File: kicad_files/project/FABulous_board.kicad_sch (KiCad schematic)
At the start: 5 parts, among them P1 USB_C_Plug_USB2.0

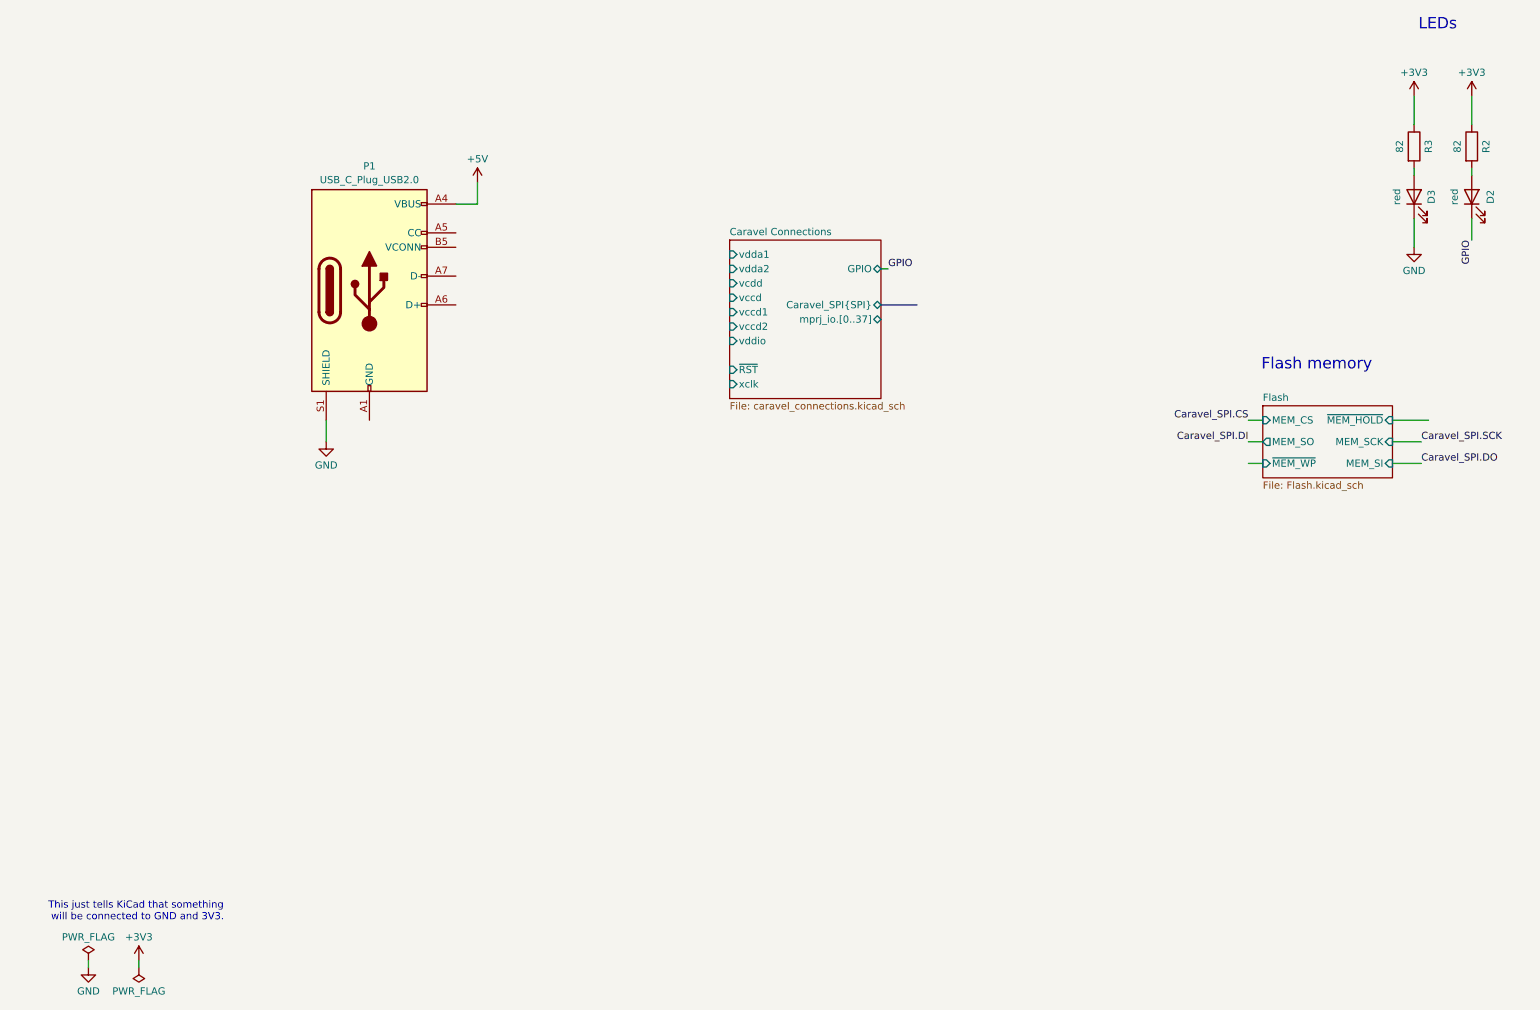
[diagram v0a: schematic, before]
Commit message: feat: schematic almost done, also add all footprints and symbol libraries except for external libraries
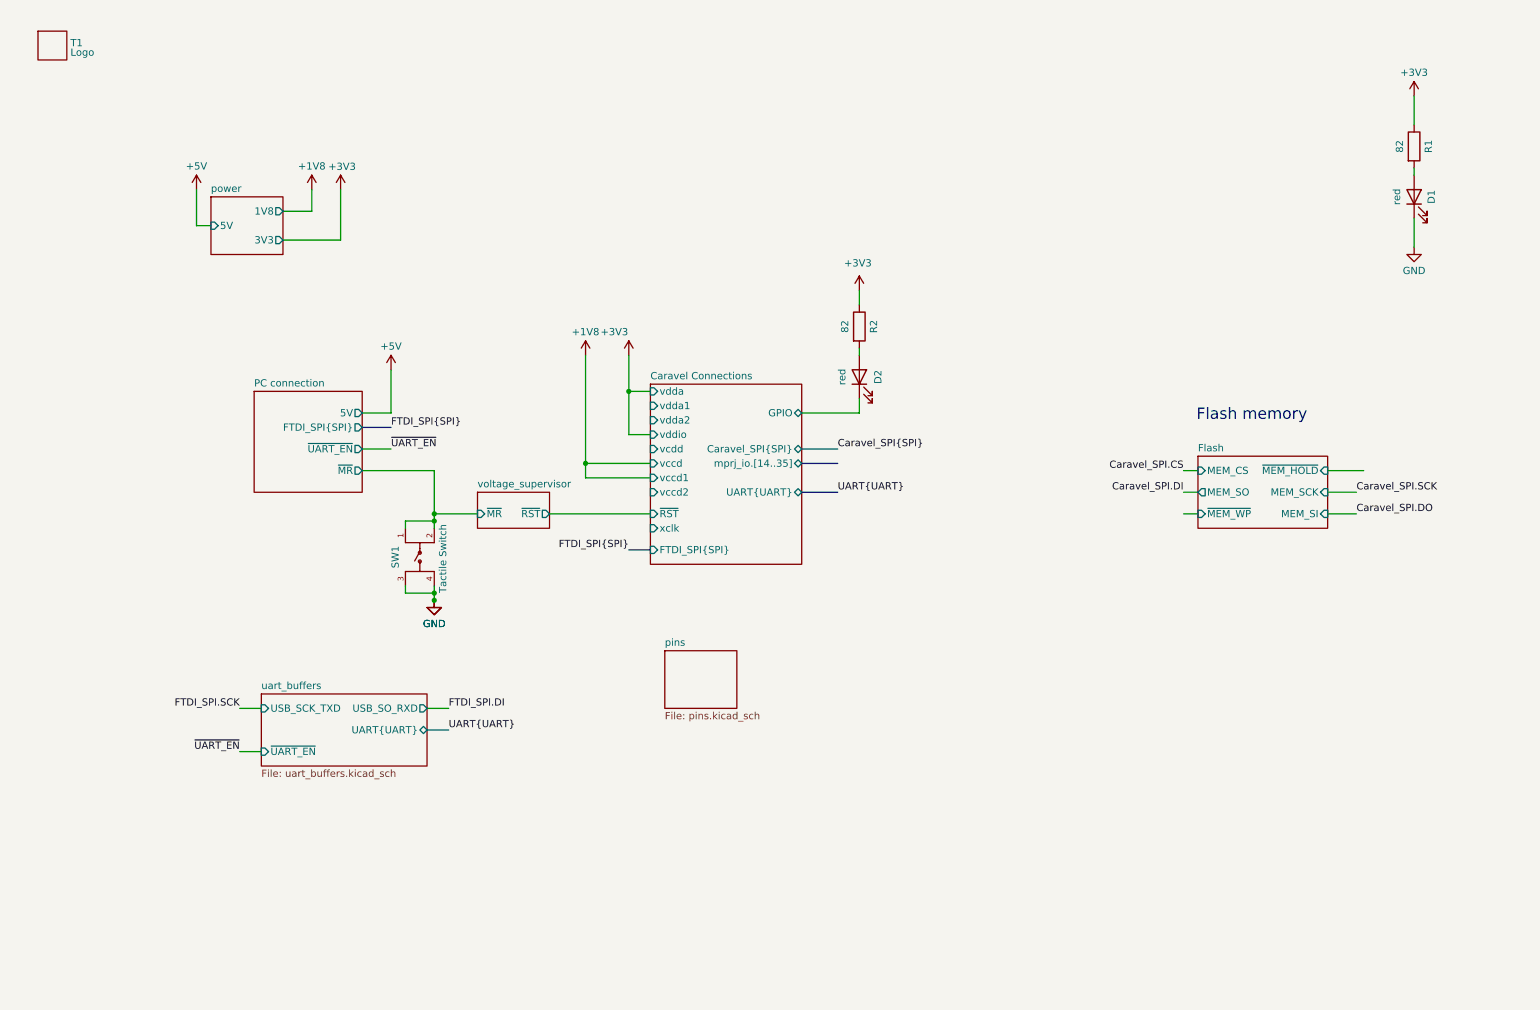
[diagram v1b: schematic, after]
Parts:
- removed P1: USB_C_Plug_USB2.0, symbol Connector:USB_C_Plug_USB2.0
- added SW1: Tactile Switch, easy_eda:SW_SMD_4P_L6.0_W6.0-P4.5-LS8.6, symbol easy_eda:Tactile Switch
- added T1: Logo, FABulous:logo, symbol FABulous:logo
- renumbered D3 to D1, R3 to R1
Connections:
- net GND: now also SW1.3, SW1.4
- net GPIO renamed Caravel Connections/GPIO
- new net PC connection/~{MR}: SW1.1, SW1.2
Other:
- added sheet PC connection (pc_connection.kicad_sch)
- added sheet pins (pins.kicad_sch)
- added sheet power (power.kicad_sch)
- added sheet uart_buffers (uart_buffers.kicad_sch)
- added sheet voltage_supervisor (voltage_supervisor.kicad_sch)
- sheet Caravel Connections ports: added FTDI_SPI{SPI}, UART{UART}, mprj_io.[14..35], vdda; removed mprj_io.[0..37]
- note removed: "LEDs"
- note removed: "This just tells KiCad that something will be connected to GND and 3V3."
- moved on the sheet: D2, R2

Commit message: started with board layout, also added more stuff on the schematic
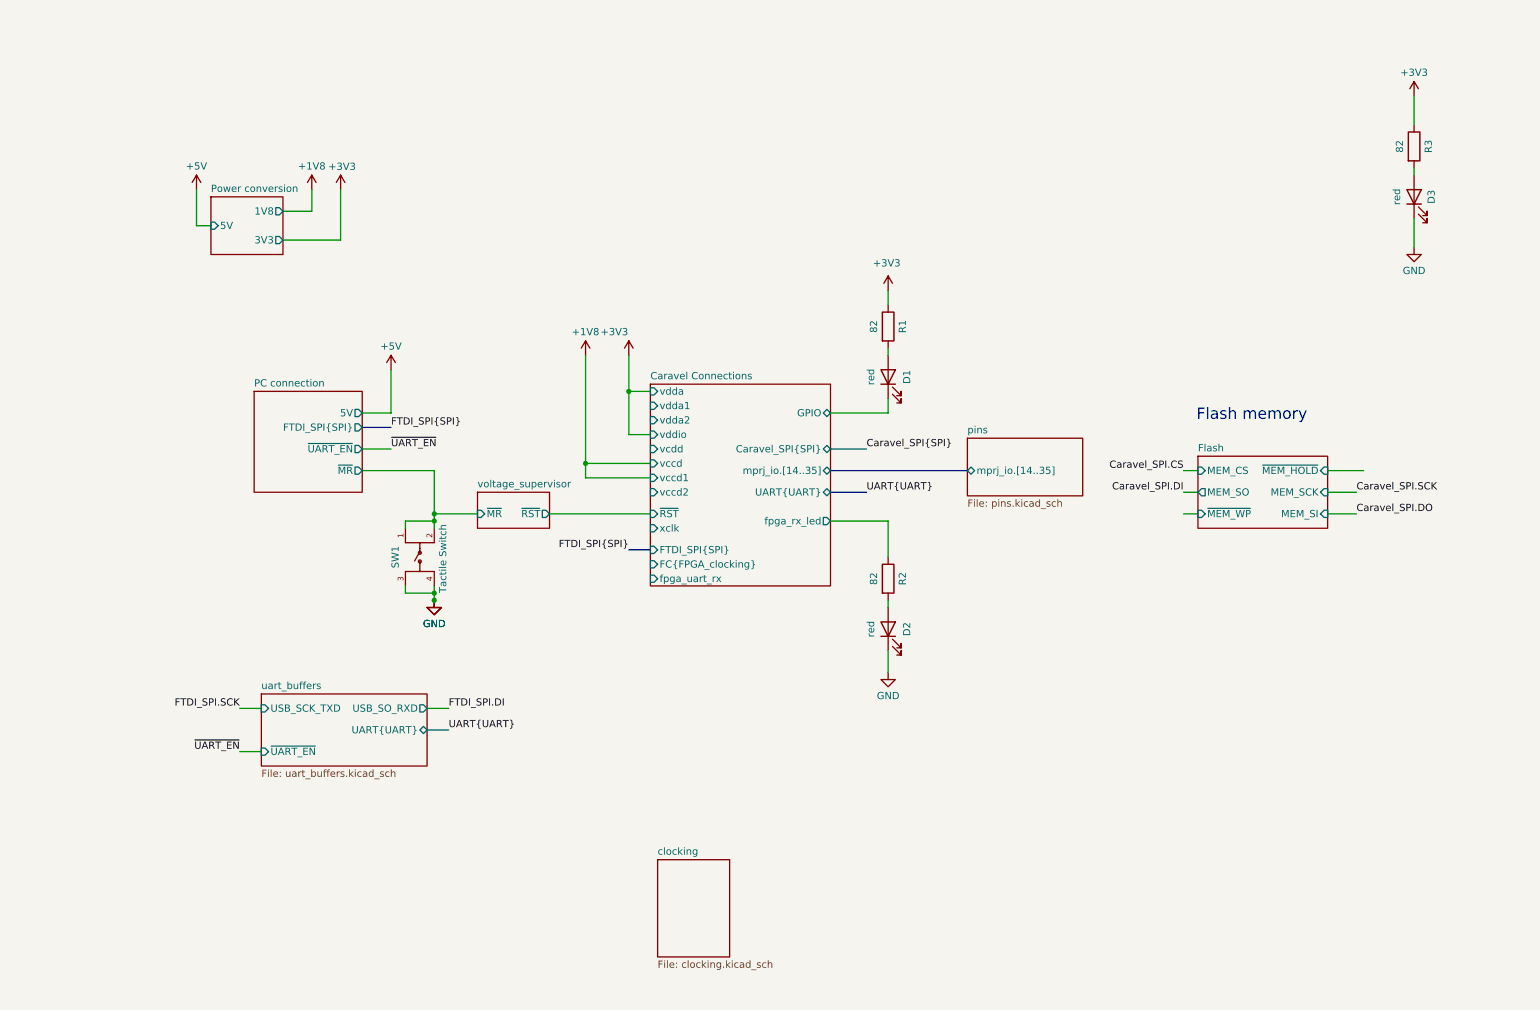
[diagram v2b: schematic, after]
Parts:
- removed T1: Logo, FABulous:logo, symbol FABulous:logo
- added D2: red, LED_SMD:LED_1206_3216Metric, symbol Device:LED
- added R2: 82, Resistor_SMD:R_0805_2012Metric, symbol Device:R
- renumbered D2 to D1, D1 to D3, R2 to R1, R1 to R3
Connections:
- net GND: now also D2.1 (K)
- new net: D2.2 (A), R2.2
- new net Caravel Connections/fpga_rx_led: R2.1
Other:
- sheet power renamed Power conversion
- added sheet clocking (clocking.kicad_sch)
- sheet Caravel Connections ports: added FC{FPGA_clocking}, fpga_rx_led, fpga_uart_rx; removed none
- sheet pins ports: added mprj_io.[14..35]; removed none
- moved on the sheet: D1, R1

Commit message: clocking IC to the schematic with all needed connections, clocks still have to be connected
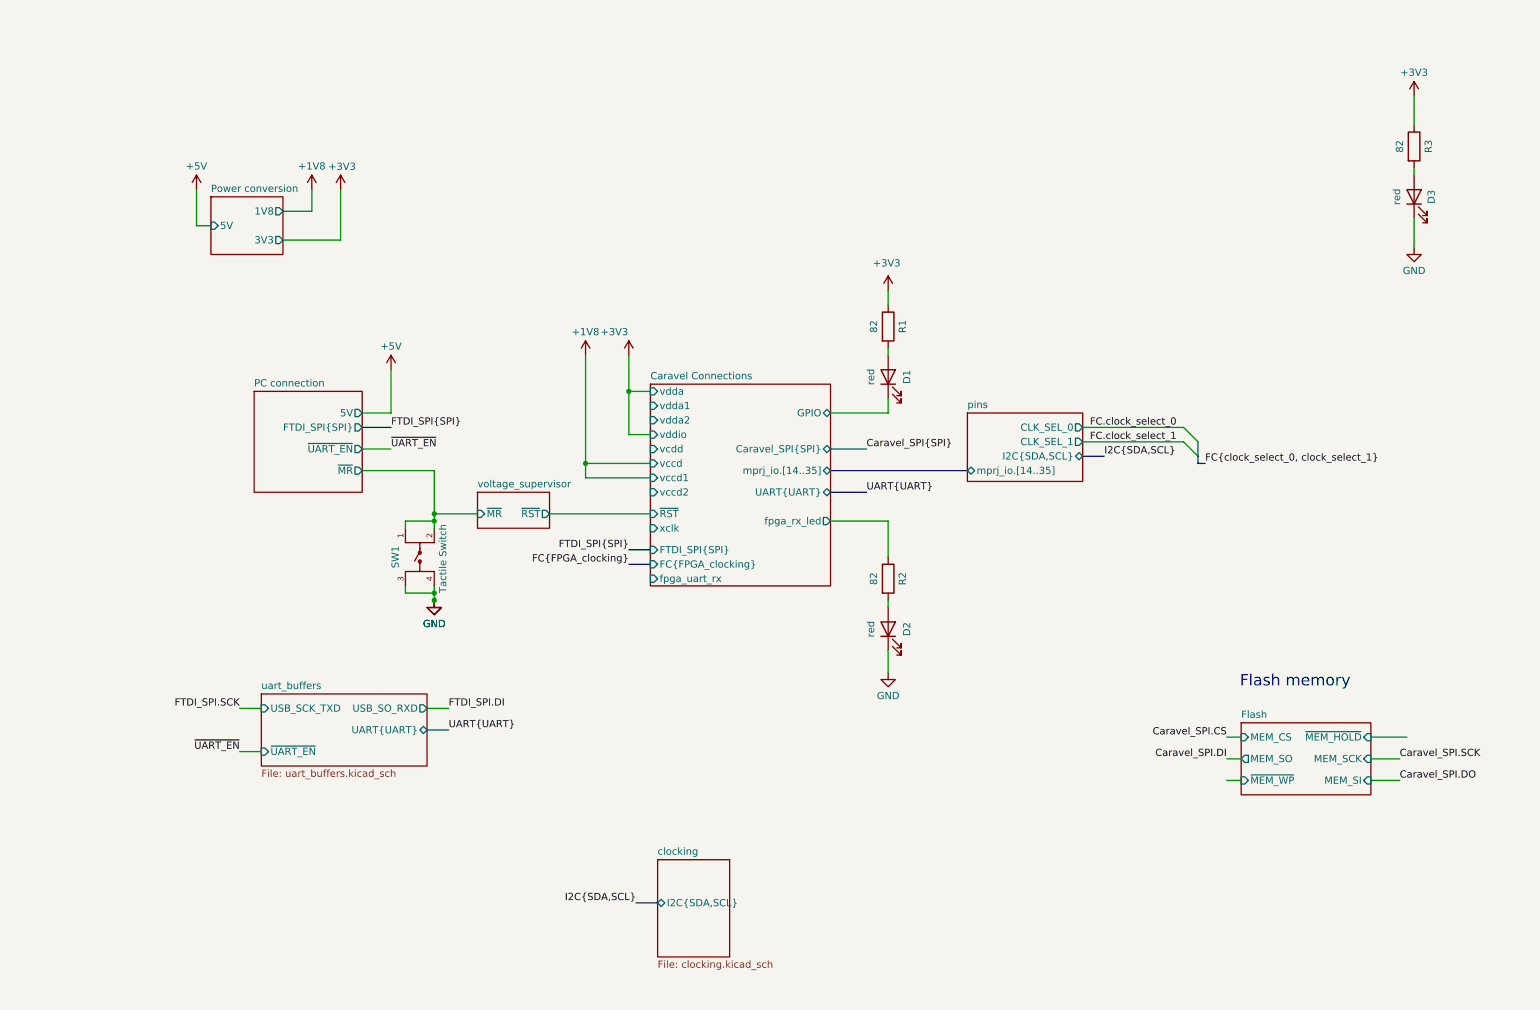
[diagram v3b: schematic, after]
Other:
- sheet clocking ports: added I2C{SDA,SCL}; removed none
- sheet pins ports: added CLK_SEL_0, CLK_SEL_1, I2C{SDA,SCL}; removed none

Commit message: new layout, add more pin header, change the caravel power pin supply
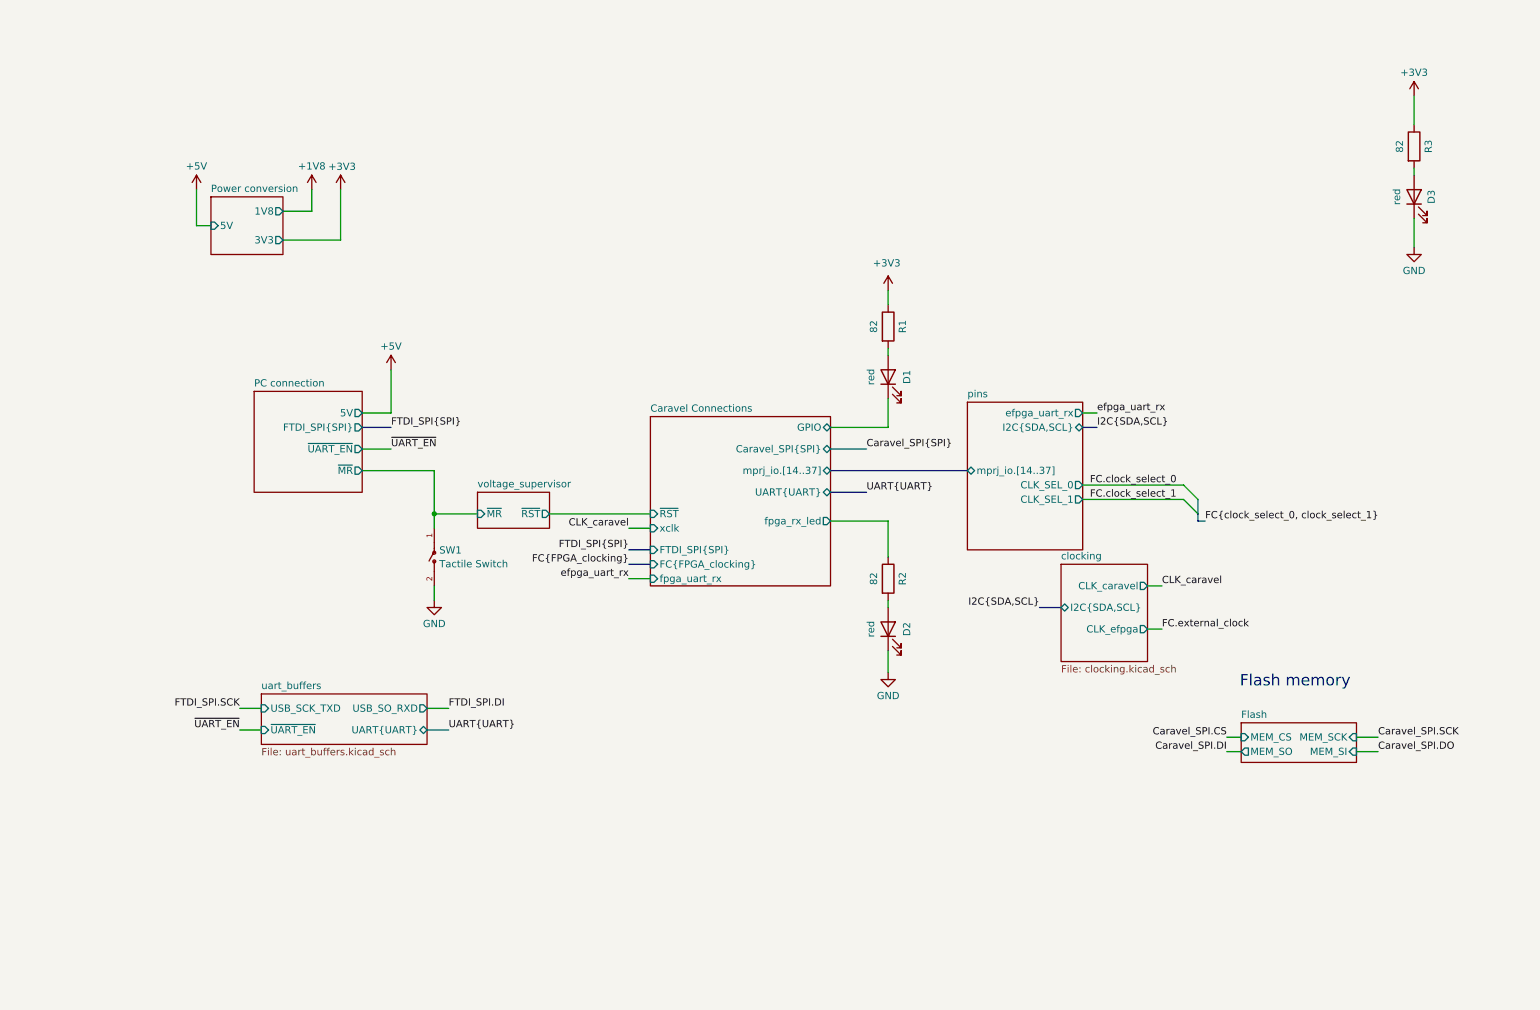
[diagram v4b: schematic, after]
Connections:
- net GND: now also SW1.2; no longer SW1.3
- net PC connection/~{MR}: now also SW1.3; no longer SW1.2
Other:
- sheet Caravel Connections ports: added mprj_io.[14..37]; removed mprj_io.[14..35], vccd, vccd1, vccd2, vcdd, vdda, vdda1, vdda2, vddio
- sheet Flash ports: added none; removed ~{MEM_HOLD}, ~{MEM_WP}
- sheet clocking ports: added CLK_caravel, CLK_efpga; removed none
- sheet pins ports: added efpga_uart_rx, mprj_io.[14..37]; removed mprj_io.[14..35]

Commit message: misc: simplifiy power pins and other components, add test pins
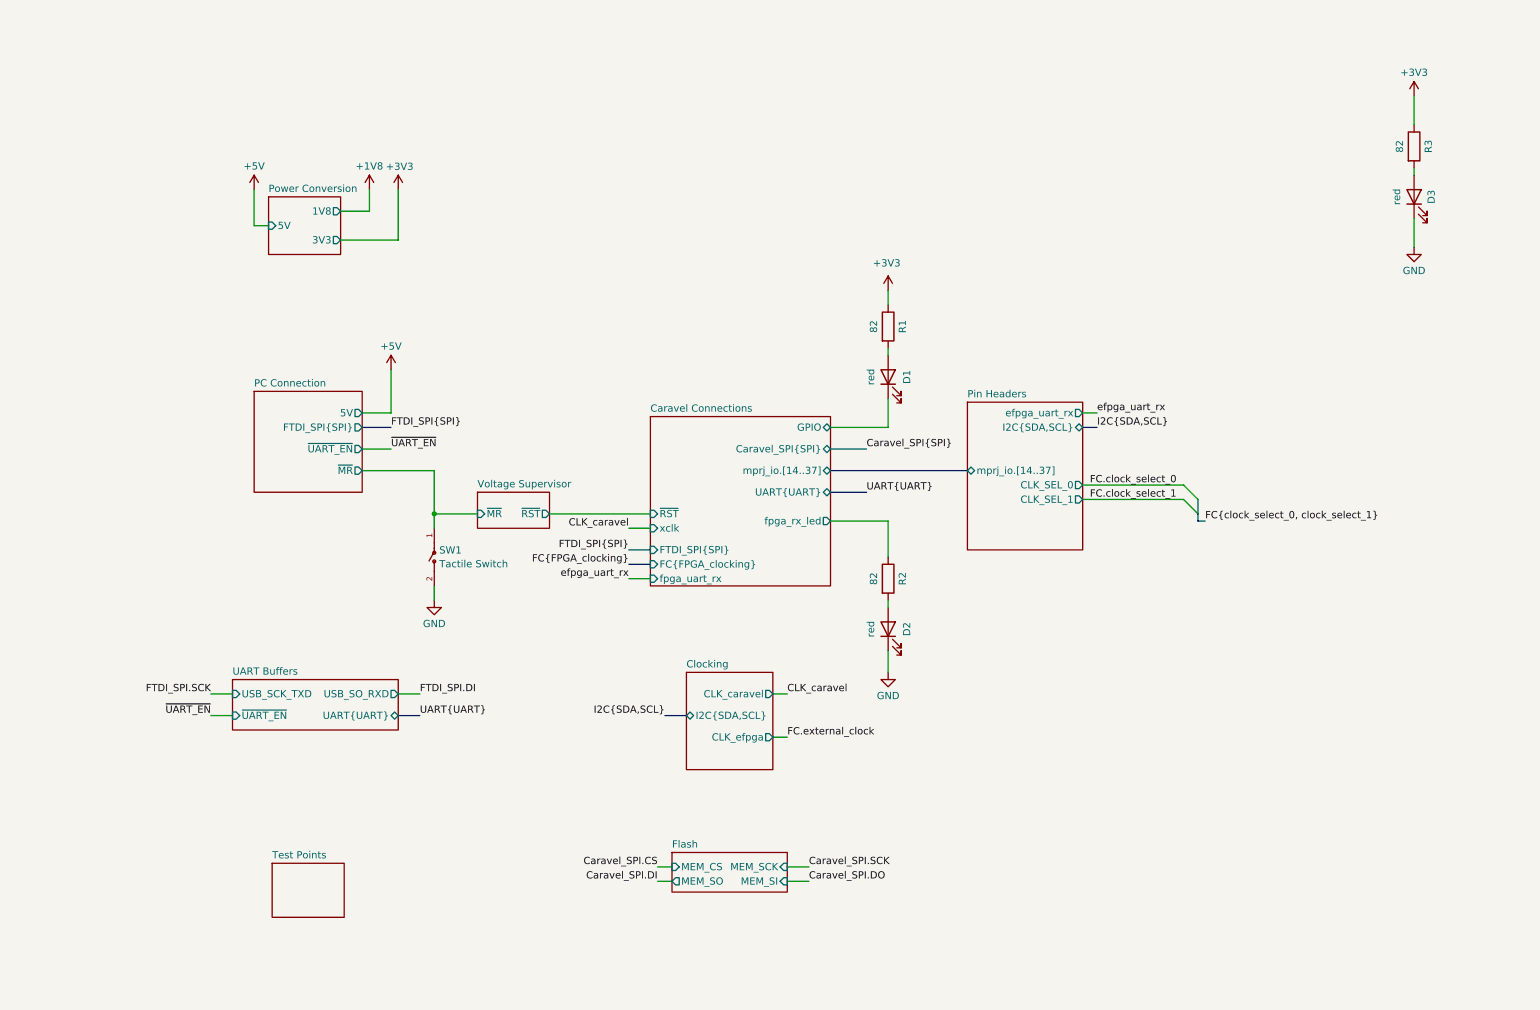
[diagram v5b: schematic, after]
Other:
- sheet PC connection renamed PC Connection
- sheet Power conversion renamed Power Conversion
- sheet clocking renamed Clocking
- sheet pins renamed Pin Headers
- sheet uart_buffers renamed UART Buffers
- sheet voltage_supervisor renamed Voltage Supervisor
- added sheet Test Points (test_points.kicad_sch)
- note removed: "Flash memory"
- title: FABulous board -> FABulous Board
